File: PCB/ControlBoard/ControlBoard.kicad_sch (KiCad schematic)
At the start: 17 parts, among them J5 PortA, J6 PortB, J7 PortC, J8 ICSP, J9 Interconnect, Q1 Q_NMOS_GSD, SW1 CONFIG, U2 PIC18F57Q84

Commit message: First pass of PCB rework.
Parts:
- removed SW1: CONFIG, Button_Switch_SMD:SW_DIP_SPSTx02_Slide_6.7x6.64mm_W8.61mm_P2.54mm_LowProfile, symbol Switch:SW_DIP_x02
- added C13: 0.1μF, Capacitor_SMD:C_0603_1608Metric, symbol Device:C_Small
- added H1, H2, H3, H4: MountingHole, MountingHole:MountingHole_3.2mm_M3, symbol Mechanical:MountingHole
- added J3: UART, Connector_PinHeader_2.54mm:PinHeader_1x03_P2.54mm_Vertical, symbol Connector_Generic:Conn_01x03
- added R14: 47k, Resistor_SMD:R_0603_1608Metric, symbol Device:R_Small
- added SW1: MODE, KTANE:SW_EVQ-P7J01P, symbol Switch:SW_SPST
- C2, C3, C7: footprint Capacitor_SMD:C_0805_2012Metric -> Capacitor_SMD:C_0603_1608Metric
- D3: footprint Diode_SMD:D_0805_2012Metric -> Diode_SMD:D_0603_1608Metric
- J5: value PortA -> Port A; footprint Custom:PinHeader_2x08_P2.54mm_Vertical-Centered -> KTANE:PinHeader_2x08_P2.54mm_Controller_With_Hole
- J6: value PortB -> Port B; footprint Custom:PinHeader_2x08_P2.54mm_Vertical-Centered -> KTANE:PinHeader_2x08_P2.54mm_Controller_With_Hole
- J7: value PortC -> Port C; footprint Custom:PinHeader_2x08_P2.54mm_Vertical-Centered -> KTANE:PinHeader_2x08_P2.54mm_Controller_With_Hole
- J9: footprint (none) -> Connector_Dsub:DSUB-9_Male_Vertical_P2.77x2.84mm
- R10, R11, R13, R8: footprint Resistor_SMD:R_0805_2012Metric -> Resistor_SMD:R_0603_1608Metric
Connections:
- net +3.3V: now also R14.1
- net ARGB-CS: now also U2.3 (RD5); no longer U2.45 (RD3)
- net BUZZER: now also U2.29 (RE2); no longer U2.17 (RB5)
- net CANRX: now also U2.9 (RB1); no longer U2.8 (RB0)
- net CANTX: now also U2.10 (RB2); no longer U2.9 (RB1)
- net CHASSIS-POS: now also U2.17 (RB5); no longer U2.10 (RB2)
- net GND: now also C13.2, J3.3 (Pin_3), SW1.2 (B)
- net SD-CS: now also U2.45 (RD3); no longer U2.2 (RD4)
- net SD-DET: now also U2.8 (RB0); no longer U2.3 (RD5)
- net SD-PWR: now also U2.2 (RD4); no longer U2.4 (RD6)
- net UART-RX: now reaches U2.5 (RD7)
- net UART-RX: now also J3.2 (Pin_2)
- net +BATT renamed VBUS
- net CONFIG1 renamed RESET/MODE
- net RESET/MODE: now also C13.1, R14.2, SW1.1 (A)
- net CONFIG2: no longer names the net of U2.28 (RE1)
- new net UART-TX: J3.1 (Pin_1), U2.4 (RD6)
- no-connect marks 7 -> 6
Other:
- note added: "Mounting"
- note added: "UART Connector"

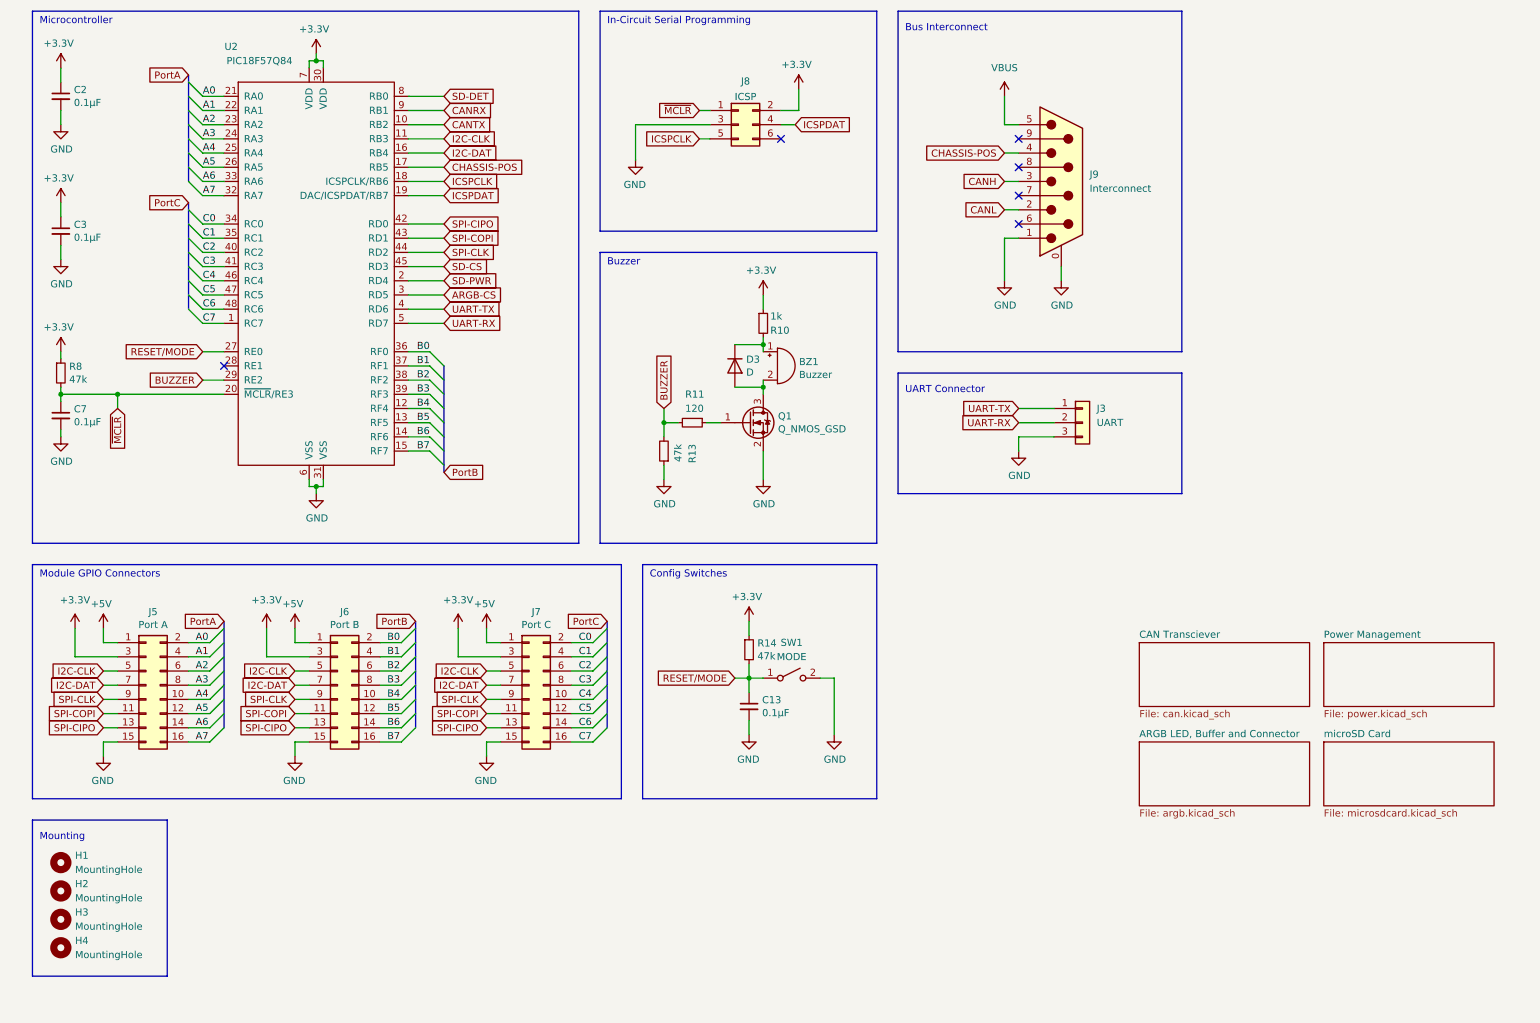
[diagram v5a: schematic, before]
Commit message: ControlBoard B02, with buck regulator fix.
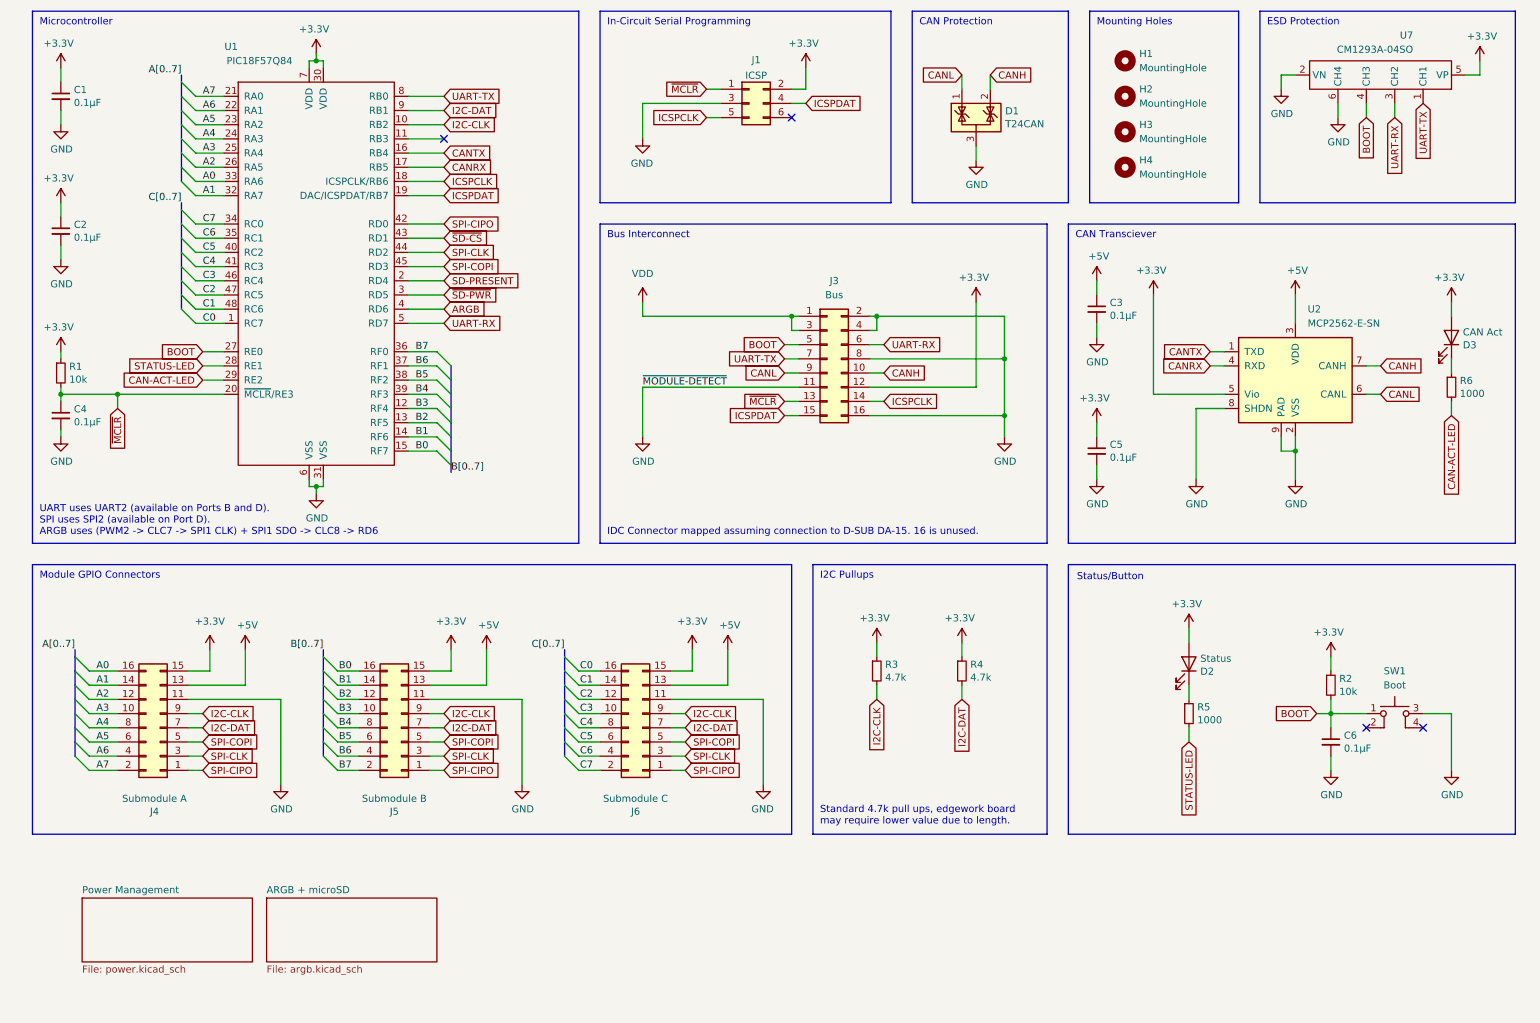
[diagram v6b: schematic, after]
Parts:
- removed BZ1: Buzzer, Buzzer_Beeper:MagneticBuzzer_CUI_CMT-8504-100-SMT, symbol Device:Buzzer
- removed C13: 0.1μF, Capacitor_SMD:C_0603_1608Metric, symbol Device:C_Small
- removed D3: D, Diode_SMD:D_0603_1608Metric, symbol Device:D
- removed J3: UART, Connector_PinHeader_2.54mm:PinHeader_1x03_P2.54mm_Vertical, symbol Connector_Generic:Conn_01x03
- removed J9: Interconnect, Connector_Dsub:DSUB-9_Male_Vertical_P2.77x2.84mm, symbol Connector:DE9_Plug_MountingHoles
- removed Q1: Q_NMOS_GSD, Package_TO_SOT_SMD:SOT-23, symbol Device:Q_NMOS_GSD
- removed R10: 1k, Resistor_SMD:R_0603_1608Metric, symbol Device:R_Small
- removed R11: 120, Resistor_SMD:R_0603_1608Metric, symbol Device:R_Small
- removed R13, R14: 47k, Resistor_SMD:R_0603_1608Metric, symbol Device:R_Small
- removed SW1: MODE, KTANE:SW_EVQ-P7J01P, symbol Switch:SW_SPST
- added C3, C5, C6: 0.1μF, Capacitor_SMD:C_0603_1608Metric, symbol Device:C_Small
- added D1: T24CAN, Package_TO_SOT_SMD:SOT-23, symbol Power_Protection:NUP2105L
- added D2: Status, LED_SMD:LED_0603_1608Metric, symbol Device:LED
- added D3: CAN Act, LED_SMD:LED_0603_1608Metric, symbol Device:LED
- added J3: Bus, KTANE:PinHeader_2x08_P2.54mm_VerticalAndHorizontal_Centered, symbol Connector_Generic:Conn_02x08_Odd_Even
- added R2: 10k, Resistor_SMD:R_0603_1608Metric, symbol Device:R_Small
- added R3, R4: 4.7k, Resistor_SMD:R_0603_1608Metric, symbol Device:R_Small
- added R5, R6: 1000, Resistor_SMD:R_0603_1608Metric, symbol Device:R_Small
- added SW1: Boot, KTANE:PTS526Sx15SMTR2xLFS, symbol KTANE:SW_Push_4Pin
- added U2: MCP2562-E-SN, Package_DFN_QFN:DFN-8-1EP_3x3mm_P0.65mm_EP1.55x2.4mm, symbol Interface_CAN_LIN:MCP2562-E-MF
- added U7: CM1293A‐04SO, Package_TO_SOT_SMD:SC-74-6_1.55x2.9mm_P0.95mm, symbol KTANE:CM1293A‐04SO
- C1: renamed from C2; DIGIKEY (none) -> 1276-1005-1-ND
- C2: renamed from C3; DIGIKEY (none) -> 1276-1005-1-ND
- C4: renamed from C7; DIGIKEY (none) -> 1276-1005-1-ND
- H1, H2, H3, H4: now left out of the parts list
- J1: renamed from J8; now left out of the parts list
- J4: renamed from J5; value Port A -> Submodule A; footprint KTANE:PinHeader_2x08_P2.54mm_Controller_With_Hole -> KTANE:PinHeader_2x08_P2.54mm_Vertical-Centered; DIGIKEY (none) -> S9171-ND
- J5: renamed from J6; value Port B -> Submodule B; footprint KTANE:PinHeader_2x08_P2.54mm_Controller_With_Hole -> KTANE:PinHeader_2x08_P2.54mm_Vertical-Centered; DIGIKEY (none) -> S9171-ND
- J6: renamed from J7; value Port C -> Submodule C; footprint KTANE:PinHeader_2x08_P2.54mm_Controller_With_Hole -> KTANE:PinHeader_2x08_P2.54mm_Vertical-Centered; DIGIKEY (none) -> S9171-ND
- R1: renamed from R8; value 47k -> 10k; DIGIKEY (none) -> P10.0KHCT-ND
- U1: renamed from U2; DIGIKEY (none) -> STOCK
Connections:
- net CHASSIS-POS is gone; now on net CANRX: U1.17 (RB5)
- net SD-CS is gone; now on net SPI-COPI: U1.45 (RD3)
- net SD-DET is gone; now on net UART-TX: U1.8 (RB0)
- net +3.3V: now also J4.15 (Pin_15), J5.15 (Pin_15), J6.15 (Pin_15), C5.1, D2.2 (A), D3.2 (A), J3.12 (Pin_12), R2.1, R3.1, R4.1, U2.5 (Vio), U7.5 (VP); no longer J4.3 (Pin_3), J5.3 (Pin_3), J6.3 (Pin_3)
- net +5V: now also J4.13 (Pin_13), J5.13 (Pin_13), J6.13 (Pin_13), C3.1, U2.3 (VDD); no longer J4.1 (Pin_1), J5.1 (Pin_1), J6.1 (Pin_1)
- net A0: now also J4.16 (Pin_16), U1.33 (RA6); no longer J4.2 (Pin_2), U1.21 (RA0)
- net A1: now also J4.14 (Pin_14), U1.32 (RA7); no longer J4.4 (Pin_4), U1.22 (RA1)
- net A2: now also J4.12 (Pin_12), U1.26 (RA5); no longer J4.6 (Pin_6), U1.23 (RA2)
- net A3: now also J4.10 (Pin_10), U1.25 (RA4); no longer J4.8 (Pin_8), U1.24 (RA3)
- net A4: now also J4.8 (Pin_8), U1.24 (RA3); no longer J4.10 (Pin_10), U1.25 (RA4)
- net A5: now also J4.6 (Pin_6), U1.23 (RA2); no longer J4.12 (Pin_12), U1.26 (RA5)
- net A6: now also J4.4 (Pin_4), U1.22 (RA1); no longer J4.14 (Pin_14), U1.33 (RA6)
- net A7: now also J4.2 (Pin_2), U1.21 (RA0); no longer J4.16 (Pin_16), U1.32 (RA7)
- net B0: now also J5.16 (Pin_16), U1.15 (RF7); no longer J5.2 (Pin_2), U1.36 (RF0)
- net B1: now also J5.14 (Pin_14), U1.14 (RF6); no longer J5.4 (Pin_4), U1.37 (RF1)
- net B2: now also J5.12 (Pin_12), U1.13 (RF5); no longer J5.6 (Pin_6), U1.38 (RF2)
- net B3: now also J5.10 (Pin_10), U1.12 (RF4); no longer J5.8 (Pin_8), U1.39 (RF3)
- net B4: now also J5.8 (Pin_8), U1.39 (RF3); no longer J5.10 (Pin_10), U1.12 (RF4)
- net B5: now also J5.6 (Pin_6), U1.38 (RF2); no longer J5.12 (Pin_12), U1.13 (RF5)
- net B6: now also J5.4 (Pin_4), U1.37 (RF1); no longer J5.14 (Pin_14), U1.14 (RF6)
- net B7: now also J5.2 (Pin_2), U1.36 (RF0); no longer J5.16 (Pin_16), U1.15 (RF7)
- net C0: now also J6.16 (Pin_16), U1.1 (RC7); no longer J6.2 (Pin_2), U1.34 (RC0)
- net C1: now also J6.14 (Pin_14), U1.48 (RC6); no longer J6.4 (Pin_4), U1.35 (RC1)
- net C2: now also J6.12 (Pin_12), U1.47 (RC5); no longer J6.6 (Pin_6), U1.40 (RC2)
- net C3: now also J6.10 (Pin_10), U1.46 (RC4); no longer J6.8 (Pin_8), U1.41 (RC3)
- net C4: now also J6.8 (Pin_8), U1.41 (RC3); no longer J6.10 (Pin_10), U1.46 (RC4)
- net C5: now also J6.6 (Pin_6), U1.40 (RC2); no longer J6.12 (Pin_12), U1.47 (RC5)
- net C6: now also J6.4 (Pin_4), U1.35 (RC1); no longer J6.14 (Pin_14), U1.48 (RC6)
- net C7: now also J6.2 (Pin_2), U1.34 (RC0); no longer J6.16 (Pin_16), U1.1 (RC7)
- net CANH: now also D1.2 (K), J3.10 (Pin_10), U2.7 (CANH)
- net CANL: now also D1.1 (K), J3.9 (Pin_9), U2.6 (CANL)
- net CANRX: now also U2.4 (RXD); no longer U1.9 (RB1)
- net CANTX: now also U1.16 (RB4), U2.1 (TXD); no longer U1.10 (RB2)
- net GND: now also J4.11 (Pin_11), J5.11 (Pin_11), J6.11 (Pin_11), C3.2, C5.2, C6.2, D1.3 (A), J3.11 (Pin_11), J3.16 (Pin_16), J3.2 (Pin_2), J3.4 (Pin_4), J3.8 (Pin_8), SW1.3, U2.2 (VSS), U2.8 (SHDN), U2.9 (PAD), U7.2 (VN), U7.6 (CH4); no longer J4.15 (Pin_15), J5.15 (Pin_15), J6.15 (Pin_15)
- net I2C-CLK: now also J4.9 (Pin_9), J5.9 (Pin_9), J6.9 (Pin_9), U1.10 (RB2), R3.2; no longer J4.5 (Pin_5), J5.5 (Pin_5), J6.5 (Pin_5), U1.11 (RB3)
- net I2C-DAT: now also U1.9 (RB1), R4.2; no longer U1.16 (RB4)
- net ICSPCLK: now also J3.14 (Pin_14)
- net ICSPDAT: now also J3.15 (Pin_15)
- net SPI-CIPO: now also J4.1 (Pin_1), J5.1 (Pin_1), J6.1 (Pin_1); no longer J4.13 (Pin_13), J5.13 (Pin_13), J6.13 (Pin_13)
- net SPI-CLK: now also J4.3 (Pin_3), J5.3 (Pin_3), J6.3 (Pin_3); no longer J4.9 (Pin_9), J5.9 (Pin_9), J6.9 (Pin_9)
- net SPI-COPI: now also J4.5 (Pin_5), J5.5 (Pin_5), J6.5 (Pin_5); no longer J4.11 (Pin_11), J5.11 (Pin_11), J6.11 (Pin_11), U1.43 (RD1)
- net UART-RX: now also J3.6 (Pin_6), U7.3 (CH2)
- net UART-TX: now also J3.7 (Pin_7), U7.1 (CH1); no longer U1.4 (RD6)
- net ~{MCLR}: now also J3.13 (Pin_13)
- net STATUS-LED: now reaches U1.28 (RE1)
- net STATUS-LED: now also R5.2
- net ARGB-CS renamed ~{SD-PWR}
- net BUZZER renamed CAN-ACT-LED
- net CAN-ACT-LED: now also R6.2
- net RESET/MODE renamed BOOT
- net BOOT: now also C6.1, J3.5 (Pin_5), R2.2, SW1.1, U7.4 (CH3)
- net SD-PWR renamed SD-PRESENT
- new net: D2.1 (K), R5.1
- new net: D3.1 (K), R6.1
- new net ARGB: U1.4 (RD6)
- new net VDD: J3.1 (Pin_1), J3.3 (Pin_3)
- new net ~{SD-CS}: U1.43 (RD1)
- no-connect marks 6 -> 4
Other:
- sheet ARGB LED, Buffer and Connector renamed ARGB + microSD
- removed sheet CAN Transciever
- removed sheet microSD Card
- note added: "CAN Protection"
- note added: "CAN Transciever"
- note added: "ESD Protection"
- note added: "I2C Pullups"
- note added: "IDC Connector mapped assuming connection to D-SUB DA-15. 16 is unused."
- note added: "Mounting Holes"
- note added: "Standard 4.7k pull ups, edgework board may require lower value due to length."
- note added: "Status/Button"
- note added: "UART uses UART2 (available on Ports B and D). SPI uses SPI2 (available on Port D). ARGB uses (PWM2 -> CLC7 -> SPI1 CLK) + SPI1 SDO -> CLC8 -> RD6"
- note removed: "Buzzer"
- note removed: "Config Switches"
- note removed: "Mounting"
- note removed: "UART Connector"
- moved on the sheet: J1, J4, J5, J6

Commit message: Correct Digikey part numbers.
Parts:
- D1: DIGIKEY STOCK -> CDSOT23-T24CANCT-ND
- J3: DIGIKEY STOCK -> STOCK/HEADER
- U1: DIGIKEY STOCK -> 150-PIC18F57Q84-I/PT-ND
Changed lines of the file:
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@@
 			)
 		)
-		(property "DIGIKEY" "STOCK"
+		(property "DIGIKEY" "150-PIC18F57Q84-I/PT-ND"
 			(at 66.04 62.23 0)
 			(effects
@@
 			)
 		)
-		(property "DIGIKEY" "STOCK"
+		(property "DIGIKEY" "CDSOT23-T24CANCT-ND"
 			(at 184.15 34.29 0)
 			(effects
@@
 			)
 		)
-		(property "DIGIKEY" "STOCK"
+		(property "DIGIKEY" "STOCK/HEADER"
 			(at 157.48 77.47 0)
 			(effects
